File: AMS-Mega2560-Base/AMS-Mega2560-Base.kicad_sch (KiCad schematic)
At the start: 26 parts, among them J3 Conn_01x08, J4 Sense1, J5 Sense2, J6 AdafruitUltimateGPS, J7 Conn_02x03_Odd_Even, P1 Power, P10 CONN_01X01, P11 CONN_01X01, P12 CONN_01X01, P13 CONN_01X01, P2 Analog, P3 Analog, P4 Digital, P5 PWM, P6 PWM, P7 Communication, P8 CONN_01X01, P9 CONN_01X01, T1 Conn_01x08, T2 Conn_01x08, T3 Conn_01x08, T4 Conn_01x08, T5 Conn_01x08, T6 Conn_01x08

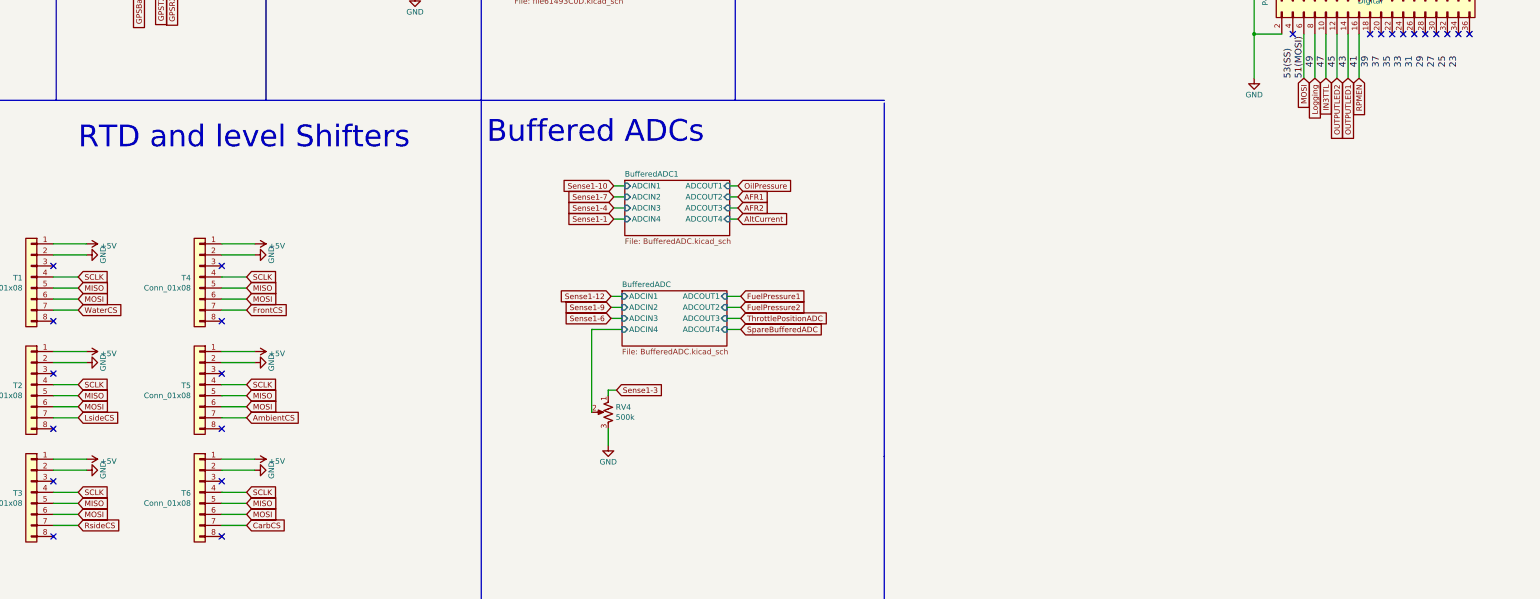
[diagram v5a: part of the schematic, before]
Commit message: updated a few things for the SPI lines to the RTDs ready for routing.
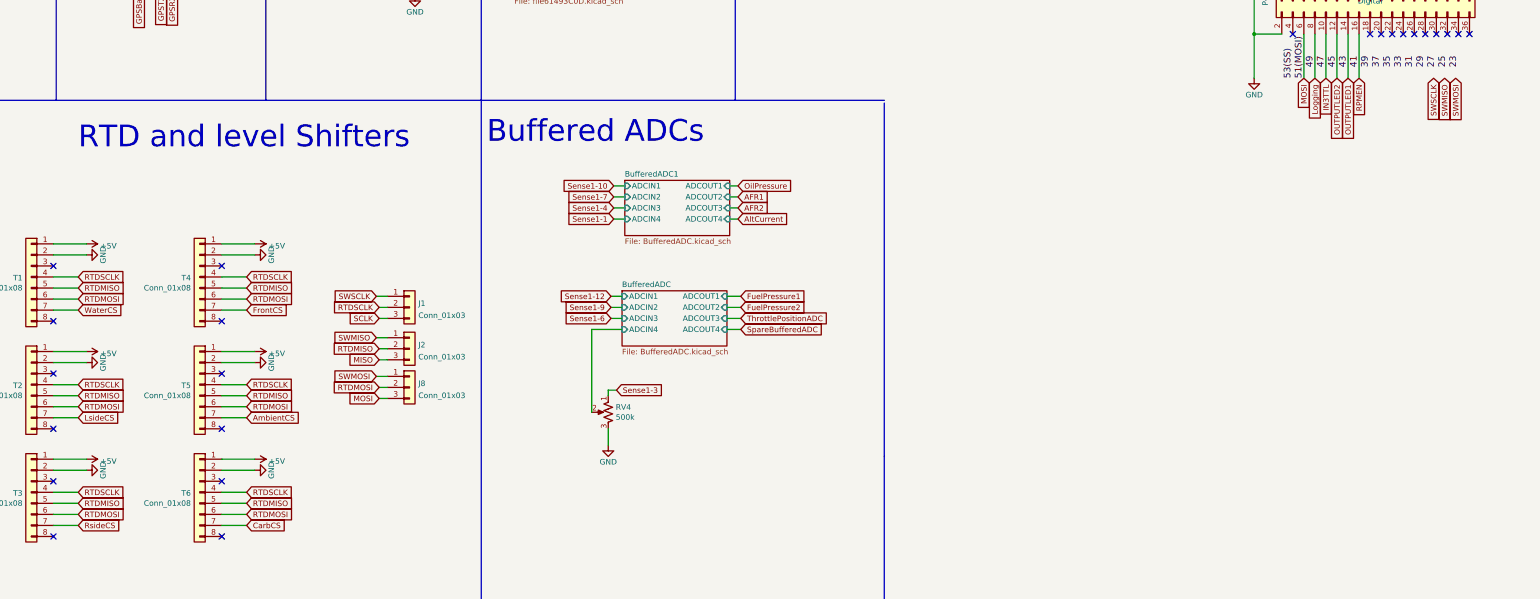
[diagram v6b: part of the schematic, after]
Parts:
- added J1, J2, J8: Conn_01x03, Connector_PinHeader_2.54mm:PinHeader_1x03_P2.54mm_Vertical, symbol Connector_Generic:Conn_01x03
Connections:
- net MISO: now also J2.3 (Pin_3); no longer T1.5 (Pin_5), T2.5 (Pin_5), T3.5 (Pin_5), T4.5 (Pin_5), T5.5 (Pin_5), T6.5 (Pin_5)
- net MOSI: now also J8.3 (Pin_3); no longer T1.6 (Pin_6), T2.6 (Pin_6), T3.6 (Pin_6), T4.6 (Pin_6), T5.6 (Pin_6), T6.6 (Pin_6)
- net SCLK: now also J1.3 (Pin_3); no longer T1.4 (Pin_4), T2.4 (Pin_4), T3.4 (Pin_4), T4.4 (Pin_4), T5.4 (Pin_4), T6.4 (Pin_4)
- new net RTDMISO: J2.2 (Pin_2), T1.5 (Pin_5), T2.5 (Pin_5), T3.5 (Pin_5), T4.5 (Pin_5), T5.5 (Pin_5), T6.5 (Pin_5)
- new net RTDMOSI: J8.2 (Pin_2), T1.6 (Pin_6), T2.6 (Pin_6), T3.6 (Pin_6), T4.6 (Pin_6), T5.6 (Pin_6), T6.6 (Pin_6)
- new net RTDSCLK: J1.2 (Pin_2), T1.4 (Pin_4), T2.4 (Pin_4), T3.4 (Pin_4), T4.4 (Pin_4), T5.4 (Pin_4), T6.4 (Pin_4)
- new net SWMISO: J2.1 (Pin_1)
- new net SWMOSI: J8.1 (Pin_1)
- new net SWSCLK: J1.1 (Pin_1)

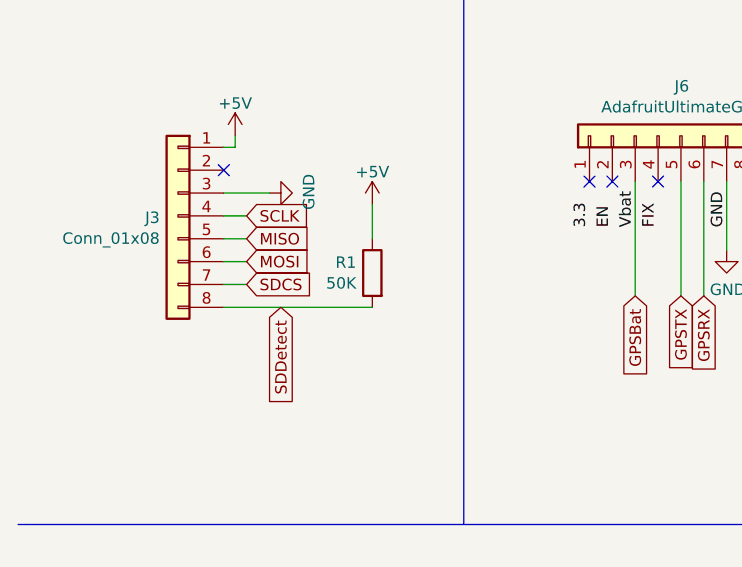
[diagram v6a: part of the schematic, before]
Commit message: updated SD Card Detect resistor to be 47k vs 50k
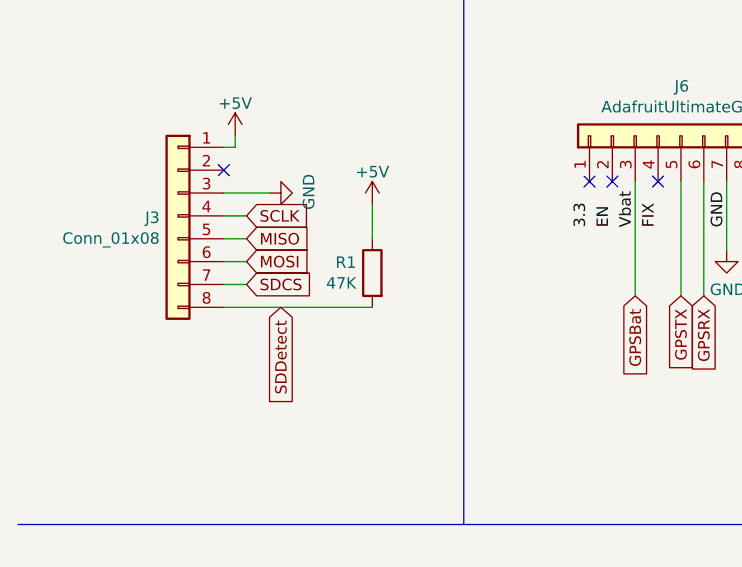
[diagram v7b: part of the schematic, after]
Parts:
- R1: value 50K -> 47K
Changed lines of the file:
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@@
       (effects (font (size 1.27 1.27)) (justify left))
     )
-    (property "Value" "50K" (id 1) (at 50.292 130.683 0)
+    (property "Value" "47K" (id 1) (at 50.292 130.683 0)
       (effects (font (size 1.27 1.27)) (justify left))
     )
@@
     )
     (path "/3055d43b-07c8-4705-873f-2885a0a28477"
-      (reference "R1") (unit 1) (value "50K") (footprint "Resistor_THT:R_Axial_DIN0207_L6.3mm_D2.5mm_P2.54mm_Vertical")
+      (reference "R1") (unit 1) (value "47K") (footprint "Resistor_THT:R_Axial_DIN0207_L6.3mm_D2.5mm_P2.54mm_Vertical")
     )
     (path "/00000000-0000-0000-0000-0000623d3962/a781b66e-4628-4987-b2c2-1aef3a4e7187"
